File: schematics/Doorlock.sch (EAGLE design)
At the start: 33 parts, among them IC1 AT90S2313P, IC2 MAX232, K1 FRS1B, K2 FRS1B

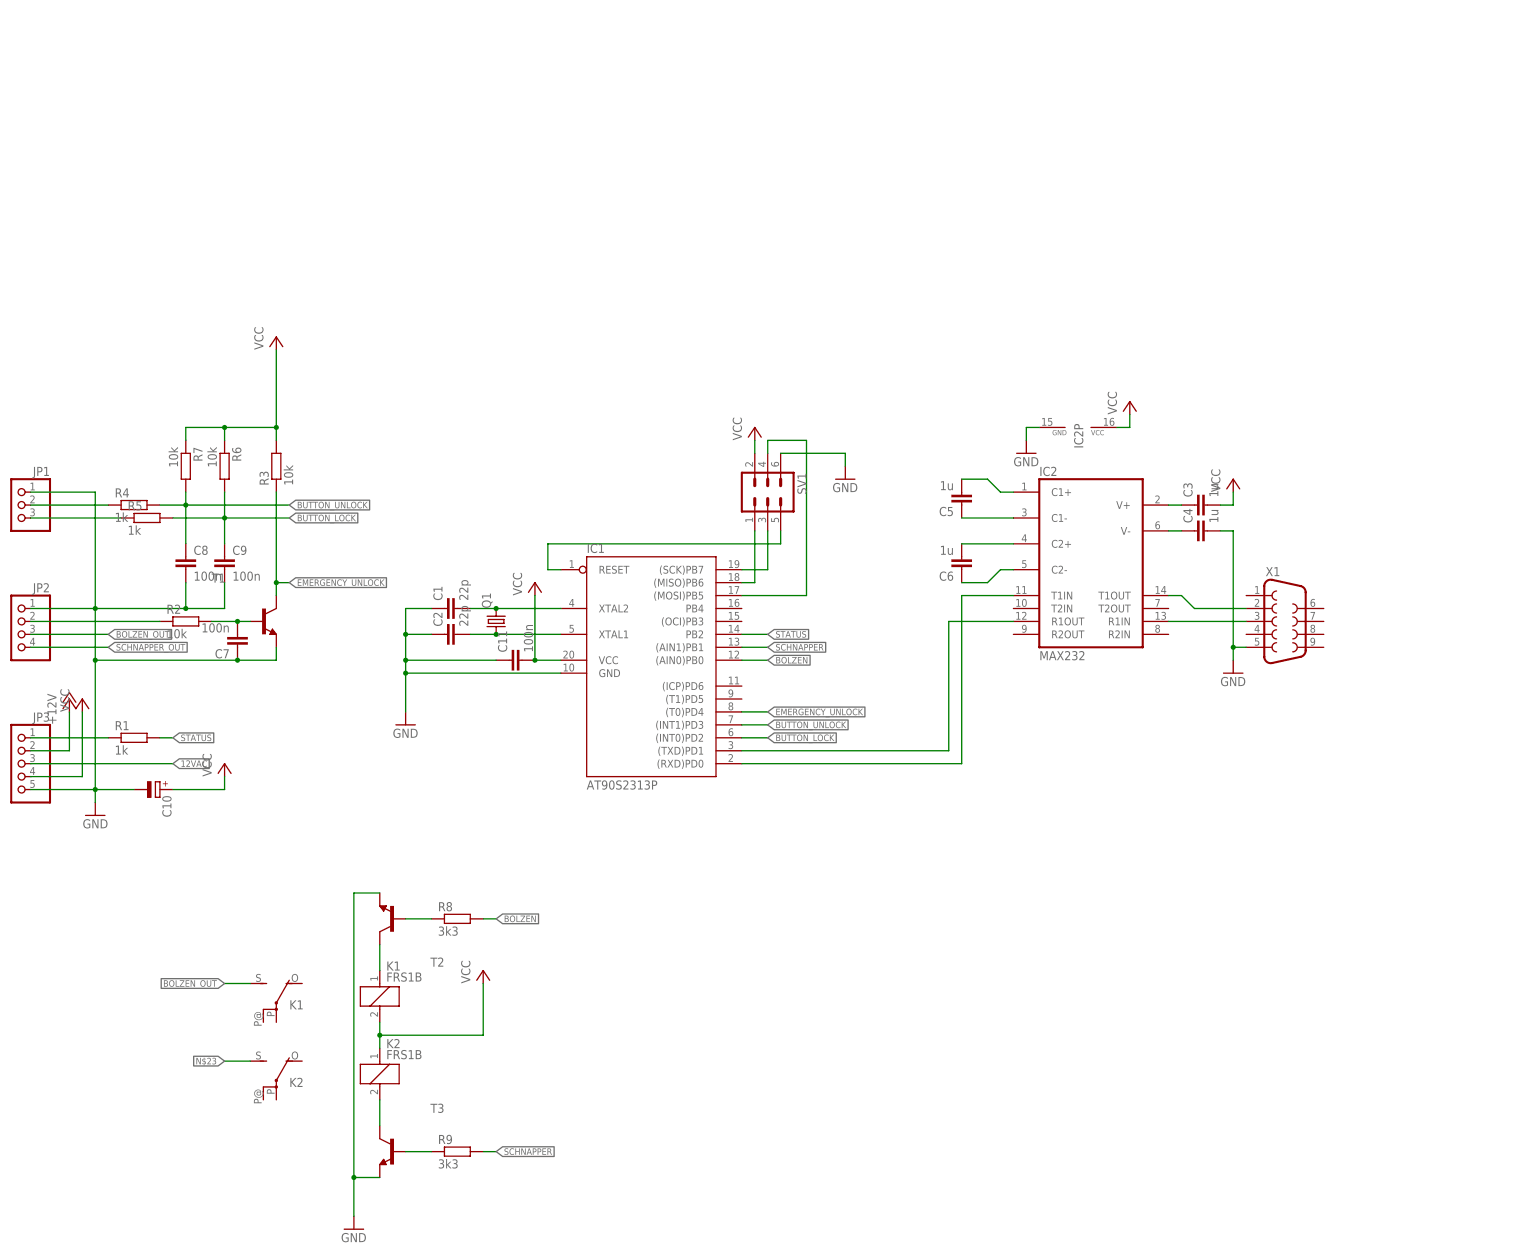
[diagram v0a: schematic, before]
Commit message: First steps towards Raspberry Pi doorlock hat
Signed-off-by: Ralf Ramsauer <ralf@binary-kitchen.de>
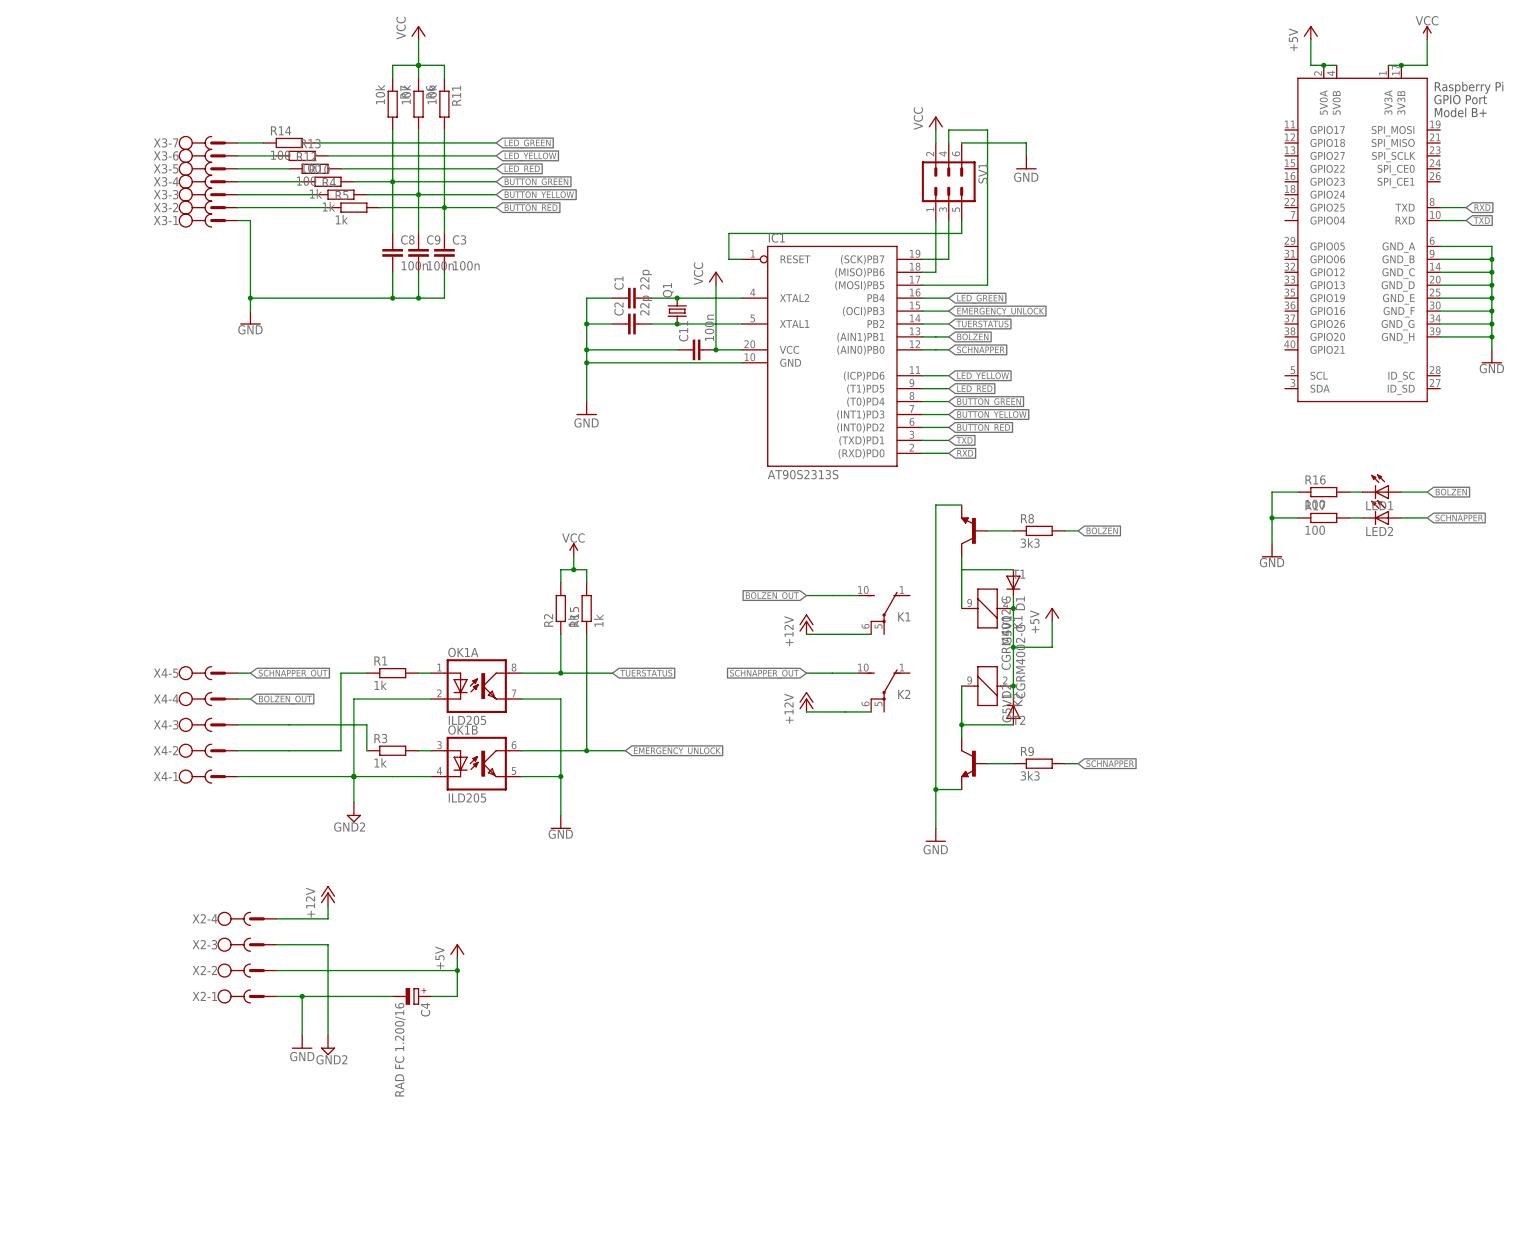
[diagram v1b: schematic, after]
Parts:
- removed C10: (no value), rcl:CPOL-EUE7.5-18
- removed C5, C6: 1u, rcl:C-EU025-024X044
- removed C7: 100n, rcl:C-EU025-024X044
- removed IC2: MAX232, maxim:MAX232
- removed JP1: (no value), pinhead:PINHD-1X3
- removed JP2: (no value), pinhead:PINHD-1X4
- removed JP3: (no value), pinhead:PINHD-1X5
- removed T3: (no value), transistor:BC337-16-NPN-TO92-CBE
- added D1, D2: CGRM4002-G, diode:CGRM4002-G
- added LED1, LED2: (no value), led:LEDCHIP-LED0805
- added OK1: ILD205, optocoupler:ILD205
- added R10, R15: 1k, rcl:R-EU_R0805
- added R11: 10k, rcl:R-EU_R0805
- added R12, R13, R14, R16, R17: 100, rcl:R-EU_R0805
- added X2: RIA182-04, con-ria182:RIA182-04
- added X3: RIA182-07, con-ria182:RIA182-07
- added X4: RIA182-05, con-ria182:RIA182-05
- C1, C11, C2, C8, C9: device rcl:C-EU025-024X044 -> rcl:C-EUC0805
- C3: value 1u -> 100n; device rcl:C-EU025-024X044 -> rcl:C-EUC0805
- C4: value 1u -> RAD FC 1.200/16; device rcl:C-EU025-024X044 -> rcl:CPOL-EUE5-10.5
- IC1: value AT90S2313P -> AT90S2313S; device atmel:AT90S2313P -> atmel:AT90S2313S
- K1, K2: value FRS1B -> G5V1; device relay:FRS1B -> relay:G5V1
- Q1: device crystal:CRYSTALHC49S -> crystal:CRYSTALHC49UP
- R1, R4, R5, R6, R7, R8, R9: device rcl:R-EU_0204/5 -> rcl:R-EU_R0805
- R2, R3: value 10k -> 1k; device rcl:R-EU_0204/5 -> rcl:R-EU_R0805
- T1: device transistor:BC547-NPN-TO92-CBE -> transistor:BC817-16-NPN-SOT23-BEC
- T2: device transistor:BC337-16-NPN-TO92-CBE -> transistor:BC817-16-NPN-SOT23-BEC
- X1: value (none) -> RASPI_BOARD_B+#_H; device con-subd:F09HP -> raspberrypi_bastelstube_v13:RASPI_BOARD_B+#_H
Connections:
- removed net 12VAC: JP3.3
- removed net BUTTON_LOCK: C9.1, IC1.(INT0)PD2, R5.2, R6.2
- removed net BUTTON_UNLOCK: C8.1, IC1.(INT1)PD3, R4.2, R7.2
- removed net N$15: C6.1, IC2G$1.C2-
- removed net N$18: C5.2, IC2G$1.C1+
- removed net N$19: JP3.1, R1.1
- removed net N$23: K22.S
- removed net STATUS: IC1.PB2, R1.2
- new net +5V: C4.+, D1.C, D2.C, K11.1, K21.1, X1.5V0A, X1.5V0B, X2-2.SK
- new net BUTTON_GREEN: C8.1, IC1.(T0)PD4, R10.2, R7.2
- new net BUTTON_RED: C3.1, IC1.(INT0)PD2, R11.2, R5.2
- new net BUTTON_YELLOW: C9.1, IC1.(INT1)PD3, R4.2, R6.2
- new net GND2: OK1A.C, OK1B.C, X2-3.SK, X4-1.SK
- new net LED_GREEN: IC1.PB4, R14.2
- new net LED_RED: IC1.(T1)PD5, R12.2
- new net LED_YELLOW: IC1.(ICP)PD6, R13.1
- new net RXD: IC1.(RXD)PD0, X1.TXD
- new net TUERSTATUS: IC1.PB2, OK1A.COL, R2.1
- new net TXD: IC1.(TXD)PD1, X1.RXD
- net +12V: now also K12.P@1, K22.P@1, X2-4.SK; no longer JP3.2
- net BOLZEN: now also IC1.(AIN1)PB1, LED1.A; no longer IC1.(AIN0)PB0
- net BOLZEN_OUT: now also X4-4.SK; no longer JP2.3
- net EMERGENCY_UNLOCK: now also IC1.(OCI)PB3, OK1B.COL, R15.1; no longer IC1.(T0)PD4, R3.1, T1.C
- net GND: now also C3.2, C4.-, OK1A.EMIT, OK1B.EMIT, R16.1, R17.1, X1.GND_A, X1.GND_B, X1.GND_C, X1.GND_D, X1.GND_E, X1.GND_F, X1.GND_G, X1.GND_H, X2-1.SK, X3-1.SK; no longer C10.-, C4.2, C7.1, IC2P.GND, JP1.1, JP2.1, JP3.5, T3.E, X1.5
- net N$10: now also R1.1, X4-2.SK; no longer JP2.2, R2.1
- net N$11: now also R13.2, X3-6.SK; no longer C3.1, IC2G$1.V+
- net N$12: now also R14.1, X3-7.SK; no longer C4.1, IC2G$1.V-
- net N$13: now also R3.1, X4-3.SK; no longer IC1.(RXD)PD0, IC2G$1.T1IN
- net N$14: now also OK1A.A, R1.2; no longer IC1.(TXD)PD1, IC2G$1.R1OUT
- net N$16: now also LED1.C, R16.2; no longer C6.2, IC2G$1.C2+
- net N$17: now also LED2.C, R17.2; no longer C5.1, IC2G$1.C1-
- net N$20: now also X3-3.SK; no longer JP1.2
- net N$21: now also X3-2.SK; no longer JP1.3
- net N$24: now also D2.A, T2.C; no longer T3.C
- net N$25: now also D1.A, K11.2, T1.C; no longer K11.1, T2.C
- net N$27: now also T1.B; no longer T2.B
- net N$28: now also T2.B; no longer T3.B
- net N$4: now also OK1B.A, R3.2; no longer C7.2, R2.2, T1.B
- net N$8: now also R10.1, X3-4.SK; no longer IC2G$1.T1OUT, X1.2
- net N$9: now also R12.1, X3-5.SK; no longer IC2G$1.R1IN, X1.3
- net SCHNAPPER: now also IC1.(AIN0)PB0, LED2.A; no longer IC1.(AIN1)PB1
- net SCHNAPPER_OUT: now also K22.S, X4-5.SK; no longer JP2.4
- net VCC: now also R11.1, R15.2, R2.2, X1.3V3A, X1.3V3B; no longer C10.+, C3.2, IC2P.VCC, JP3.4, K11.2, K21.1, R3.2
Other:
- moved on the sheet: C1, C11, C2, C3, C8, C9, IC1, K1, K2, Q1, R1, R2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
